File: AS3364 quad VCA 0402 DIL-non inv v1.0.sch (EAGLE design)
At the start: 36 parts, among them IC1 TL072JD, IC2 TL072JD

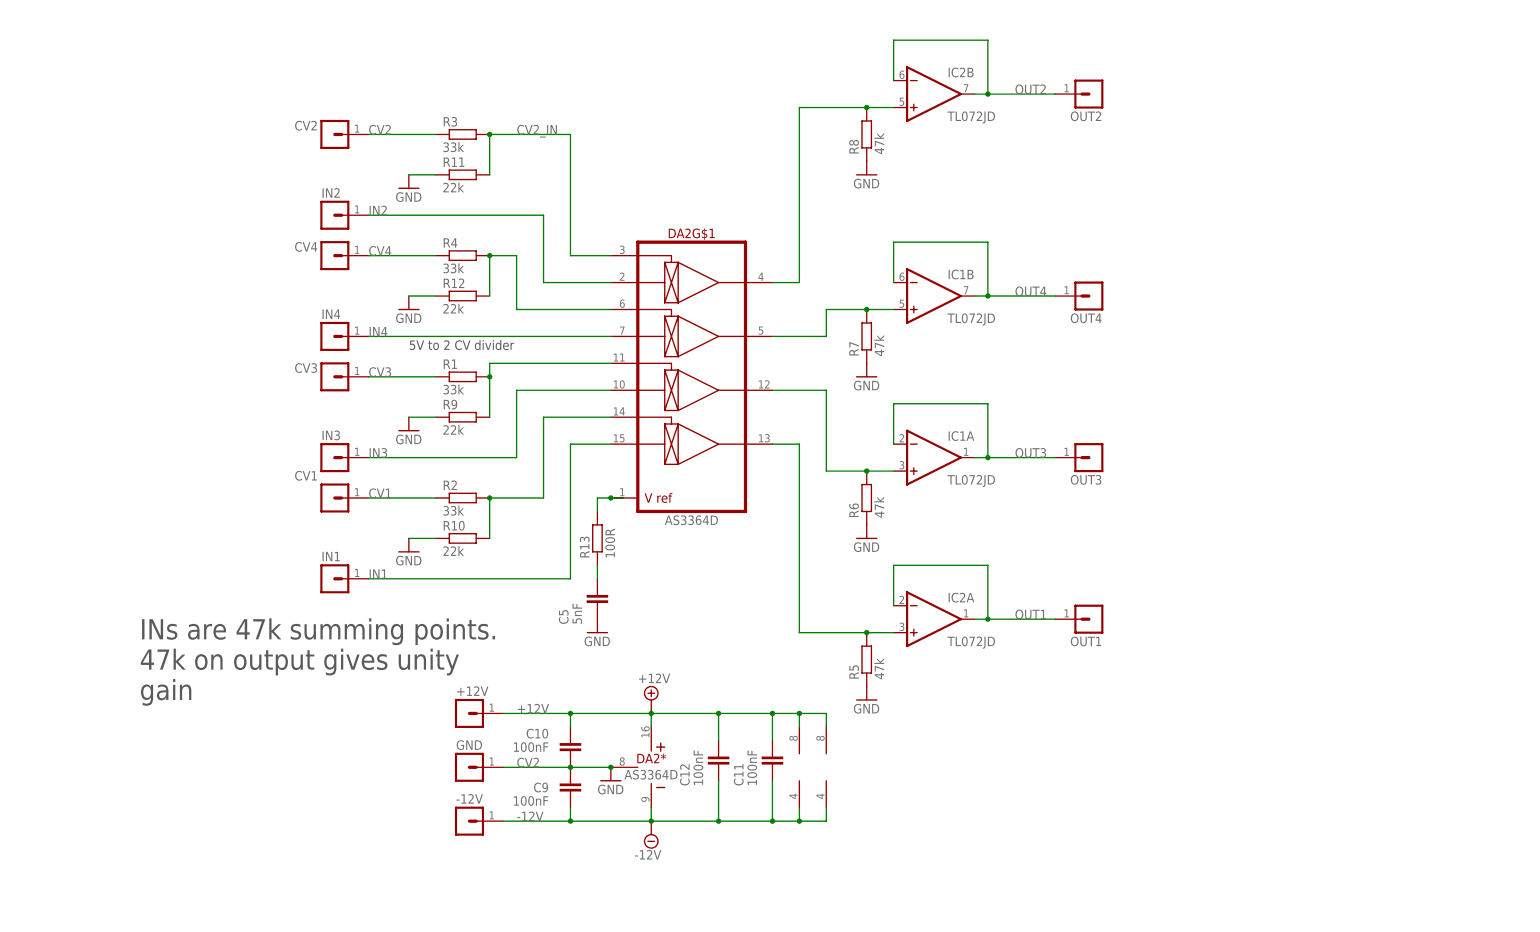
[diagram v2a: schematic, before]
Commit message: Almost finished bom/cpl
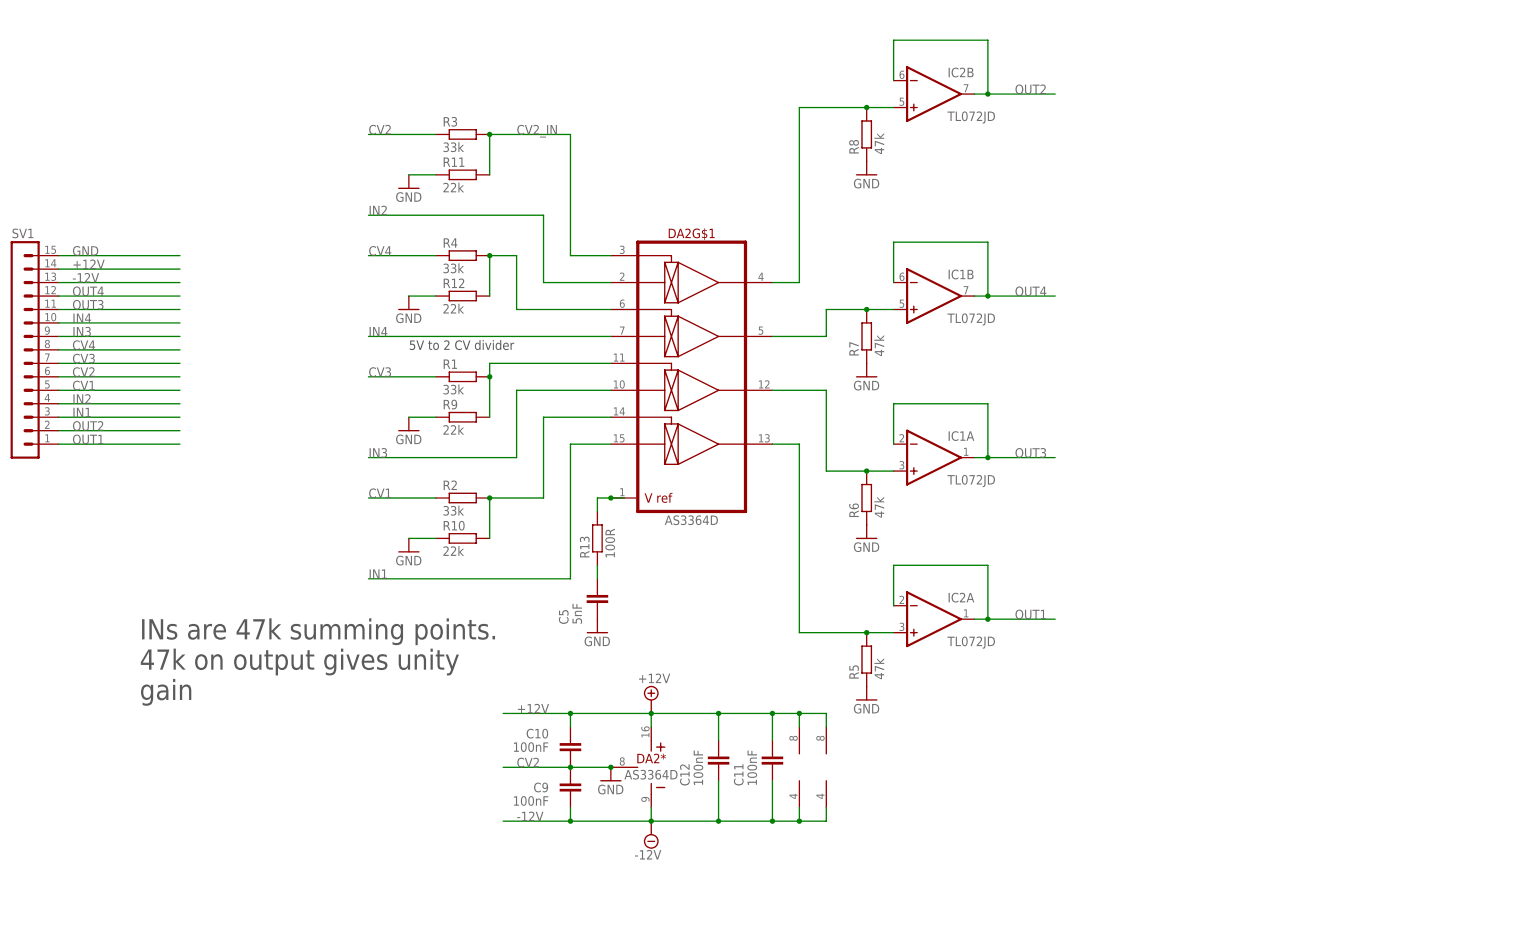
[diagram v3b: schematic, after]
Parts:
- removed +12V, -12V, CV1, CV2, CV3, CV4, GND, IN1, IN2, IN3, IN4, OUT1, OUT2, OUT3, OUT4: (no value), joakim:MA01-1JP
- added SV1: (no value), joakim:MA15-1JP
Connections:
- net +12V: now also SV1.14; no longer +12V.1
- net -12V: now also SV1.13; no longer -12V.1
- net CV1: now also SV1.5; no longer CV1.1
- net CV2: now also SV1.6; no longer CV2.1
- net CV3: now also SV1.7; no longer CV3.1
- net CV4: now also SV1.8; no longer CV4.1
- net GND: now also SV1.15; no longer GND.1
- net IN1: now also SV1.3; no longer IN1.1
- net IN2: now also SV1.4; no longer IN2.1
- net IN3: now also SV1.9; no longer IN3.1
- net IN4: now also SV1.10; no longer IN4.1
- net OUT1: now also SV1.1; no longer OUT1.1
- net OUT2: now also SV1.2; no longer OUT2.1
- net OUT3: now also SV1.11; no longer OUT3.1
- net OUT4: now also SV1.12; no longer OUT4.1
